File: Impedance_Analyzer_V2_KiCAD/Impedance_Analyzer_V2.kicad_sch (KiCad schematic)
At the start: 51 parts, among them J1 Conn_Coaxial, J10 Conn_02x02_Counter_Clockwise, J11 Screw_Terminal_01x03, J12 Conn_02x02_Counter_Clockwise, J13 Conn_02x02_Counter_Clockwise, J14 Conn_02x02_Counter_Clockwise, J15 Conn_02x02_Counter_Clockwise, J16 Conn_02x02_Counter_Clockwise, J17 Conn_02x02_Counter_Clockwise, J2 Conn_Coaxial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

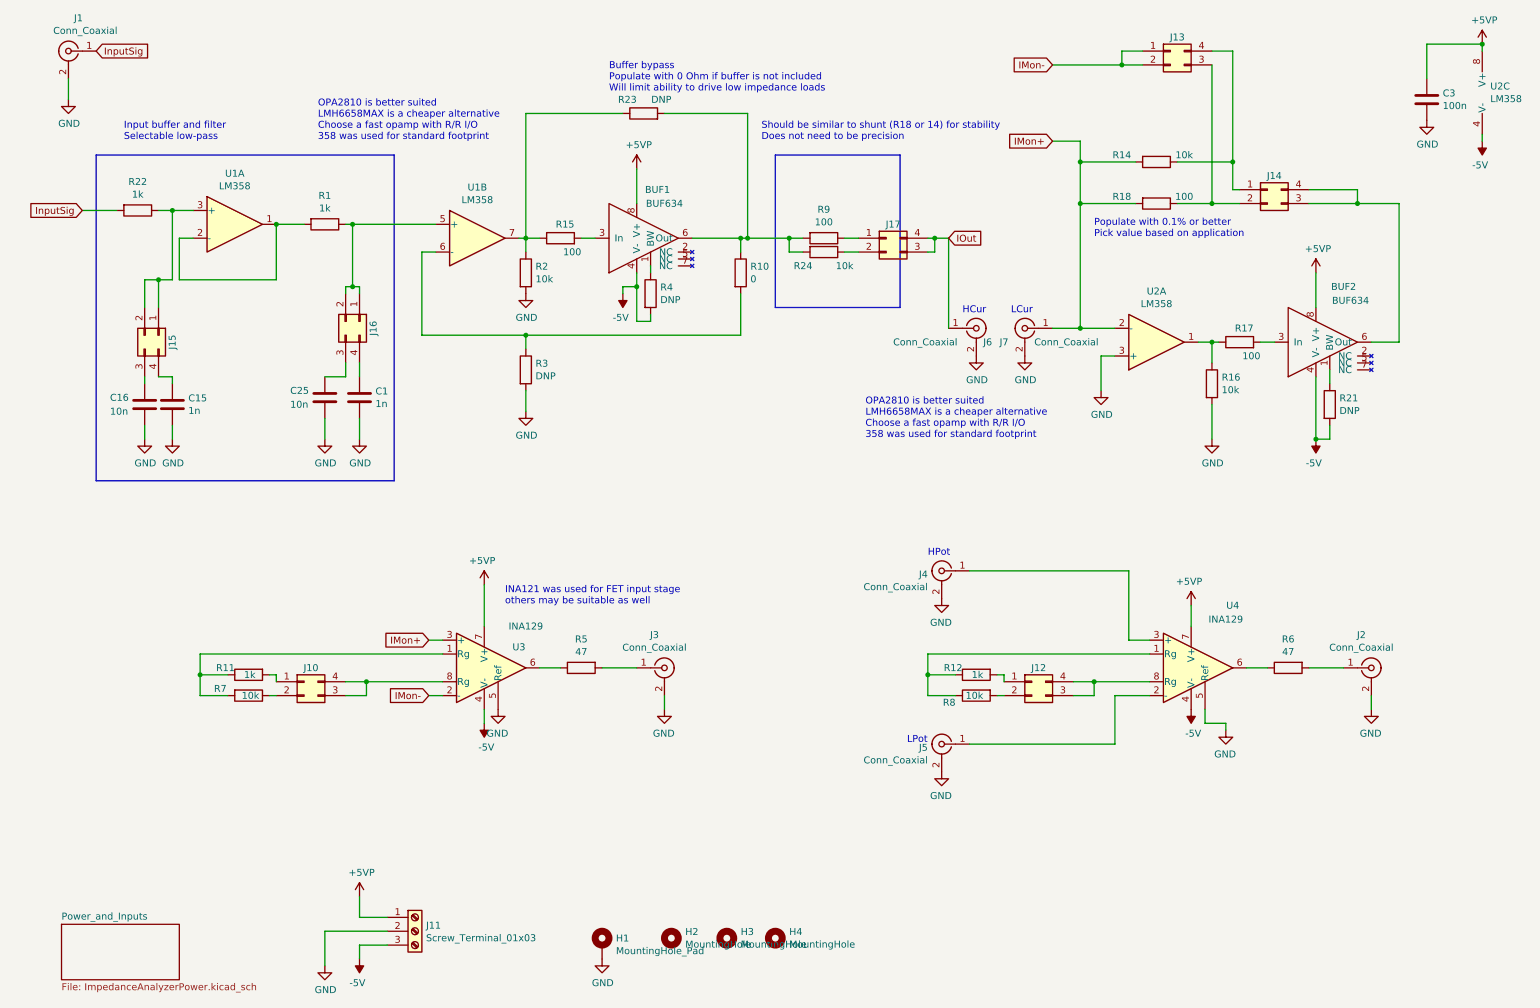
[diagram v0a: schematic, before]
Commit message: Make Rev C + Curve tracer init
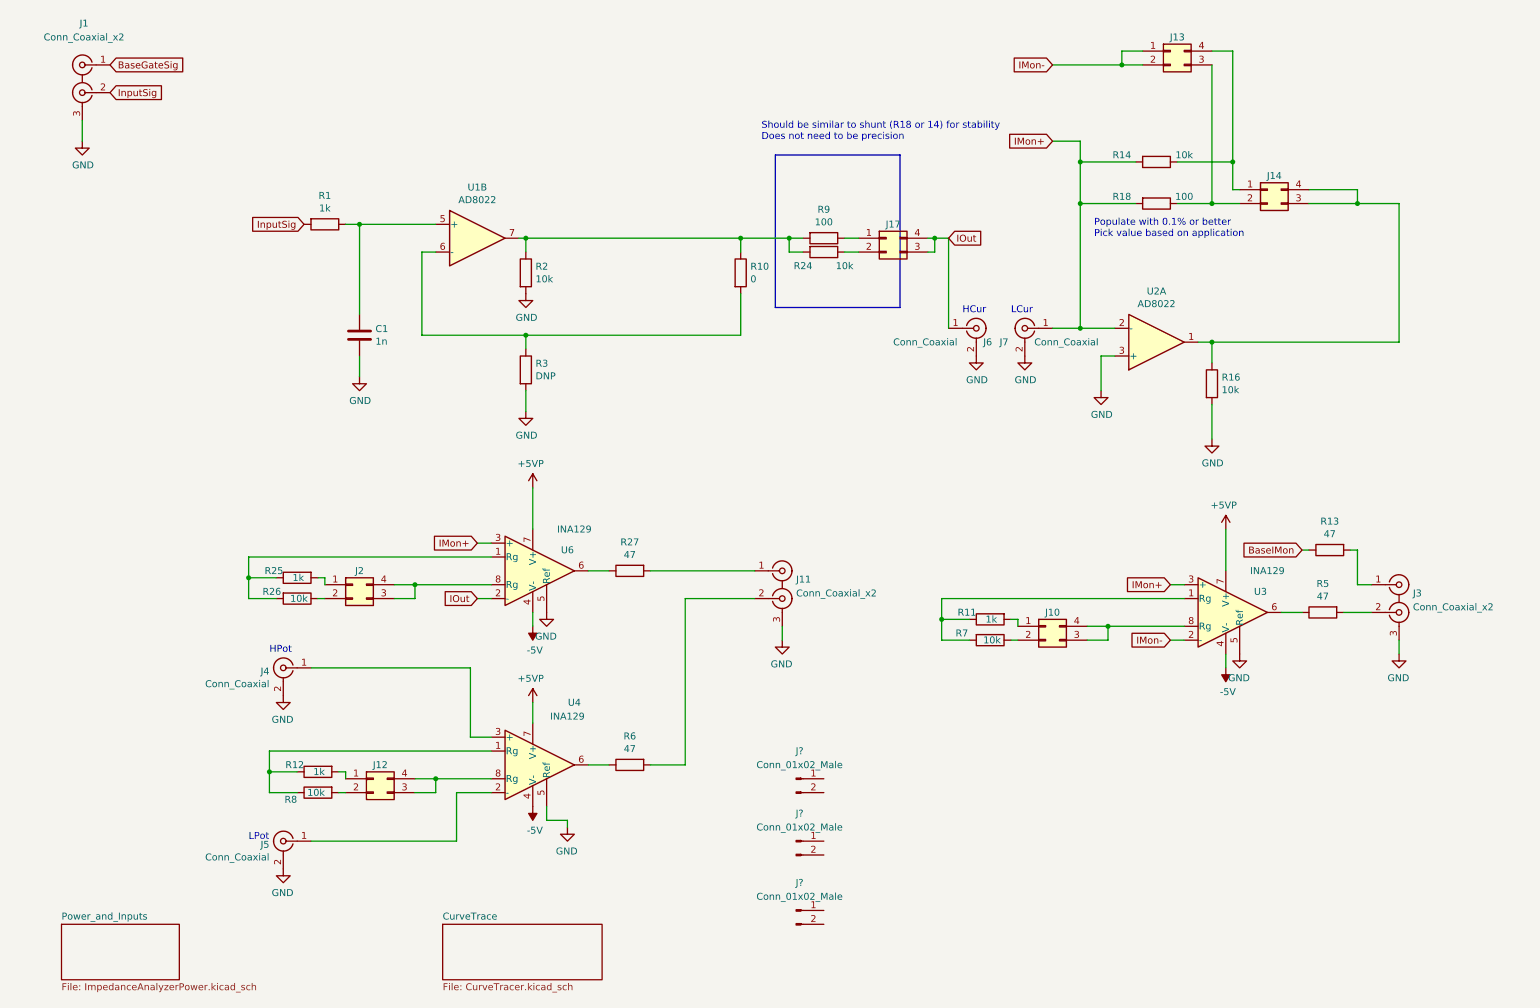
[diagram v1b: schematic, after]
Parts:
- removed BUF1, BUF2: BUF634, Package_SO:SO-8_3.9x4.9mm_P1.27mm, symbol Eli_Lib:BUF634
- removed C15: 1n, Capacitor_SMD:C_0805_2012Metric, symbol Device:C
- removed C16, C25: 10n, Capacitor_SMD:C_0805_2012Metric, symbol Device:C
- removed C3: 100n, Capacitor_SMD:C_0805_2012Metric, symbol Device:C
- removed H1: MountingHole_Pad, MountingHole:MountingHole_4.3mm_M4_Pad, symbol Mechanical:MountingHole_Pad
- removed H2, H3, H4: MountingHole, MountingHole:MountingHole_4mm, symbol Mechanical:MountingHole
- removed J1, J2, J3: Conn_Coaxial, Connector_Coaxial:BNC_TEConnectivity_1478204_Vertical, symbol Connector:Conn_Coaxial
- removed J11: Screw_Terminal_01x03, TerminalBlock:TerminalBlock_bornier-3_P5.08mm, symbol Connector:Screw_Terminal_01x03
- removed J15, J16: Conn_02x02_Counter_Clockwise, Connector_PinHeader_2.54mm:PinHeader_2x02_P2.54mm_Vertical, symbol Connector_Generic:Conn_02x02_Counter_Clockwise
- removed R15, R17: 100, Resistor_SMD:R_1206_3216Metric, symbol Device:R
- removed R21, R23, R4: DNP, Resistor_SMD:R_1206_3216Metric, symbol Device:R
- removed R22: 1k, Resistor_SMD:R_1206_3216Metric, symbol Device:R
- removed unit 1 of U1
- removed unit 3 of U2
- added J1, J11, J3: Conn_Coaxial_x2, Connector_Coaxial:BNC_Win_364A2x95_Horizontal, symbol Connector:Conn_Coaxial_x2
- added J2: Conn_02x02_Counter_Clockwise, Connector_PinHeader_2.54mm:PinHeader_2x02_P2.54mm_Vertical, symbol Connector_Generic:Conn_02x02_Counter_Clockwise
- added J? (x3): Conn_01x02_Male, symbol Connector:Conn_01x02_Male
- added R13, R27: 47, Resistor_SMD:R_1206_3216Metric, symbol Device:R
- added R25: 1k, Resistor_SMD:R_1206_3216Metric, symbol Device:R
- added R26: 10k, Resistor_SMD:R_1206_3216Metric, symbol Device:R
- added U6: INA129, Package_DIP:DIP-8_W7.62mm, symbol Amplifier_Instrumentation:INA129
- U1, U2: value LM358 -> AD8022
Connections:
- net +5VP: now also U6.7 (V+)
- net -5V: now also U6.4 (V-)
- net GND: now also J1.3 (EXT), J11.3 (EXT), J3.3 (EXT), U6.5 (Ref)
- net IMon+: now also U6.3 (+)
- net IOut: now also U6.2 (-)
- net InputSig: now also R1.2, J1.2 (IN2)
- net at R2.1, U1.7: now also R10.1, R24.2, R9.2
- net at R1.1, U1.5 (+): now also C1.1
- net at R6.2: now also J11.2 (IN2)
- net at R5.2: now also J3.2 (IN2)
- net at R16.1, U2.1: now also J14.3 (Pin_3), J14.4 (Pin_4)
- new net: J3.1 (IN1), R13.2
- new net: J2.2 (Pin_2), R26.1
- new net: R25.1, R26.2, U6.1 (Rg)
- new net: R27.1, U6.6
- new net: J11.1 (IN1), R27.2
- new net: J2.1 (Pin_1), R25.2
- new net: J2.3 (Pin_3), J2.4 (Pin_4), U6.8 (Rg)
- new net BaseGateSig: J1.1 (IN1)
- new net BaseIMon: R13.1
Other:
- added sheet CurveTrace (CurveTracer.kicad_sch)
- note removed: "Buffer bypass Populate with 0 Ohm if buffer is not included Will limit ability to drive low impedance loads"
- note removed: "INA121 was used for FET input stage others may be suitable as well"
- note removed: "Input buffer and filter Selectable low-pass"
- note removed: "OPA2810 is better suited LMH6658MAX is a cheaper alternative Choose a fast opamp with R/R I/O 358 was used for standard footprint"
- moved on the sheet: C1, J10, J12, J4, J5, R11, R12, R5, R6, R7, R8, U3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

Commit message: Update Impedance board
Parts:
- J15, J16, J18: renamed from J?; footprint (none) -> Connector_PinHeader_2.54mm:PinHeader_1x02_P2.54mm_Horizontal
- J4, J5, J6, J7: footprint Connector_Coaxial:BNC_TEConnectivity_1478204_Vertical -> Eli_Lib:31-5486-1010 BNC Panel RA
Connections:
- net IMon+: now also J18.2 (Pin_2)
- net IOut: now also J15.1 (Pin_1)
- net at J5.1 (In), U4.2 (-): now also J16.2 (Pin_2), J18.1 (Pin_1)
- net at J4.1 (In), U4.3 (+): now also J15.2 (Pin_2), J16.1 (Pin_1)
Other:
- moved on the sheet: J15, J16, J18
